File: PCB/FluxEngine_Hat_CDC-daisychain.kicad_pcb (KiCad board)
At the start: 2 copper layers, 83.3 x 24.1 mm, 3 parts, among them J1 CY8CKIT-059, P1 FDC_BUS_IBMPC, P2 FDC_BUS_CDC_DaisyChain

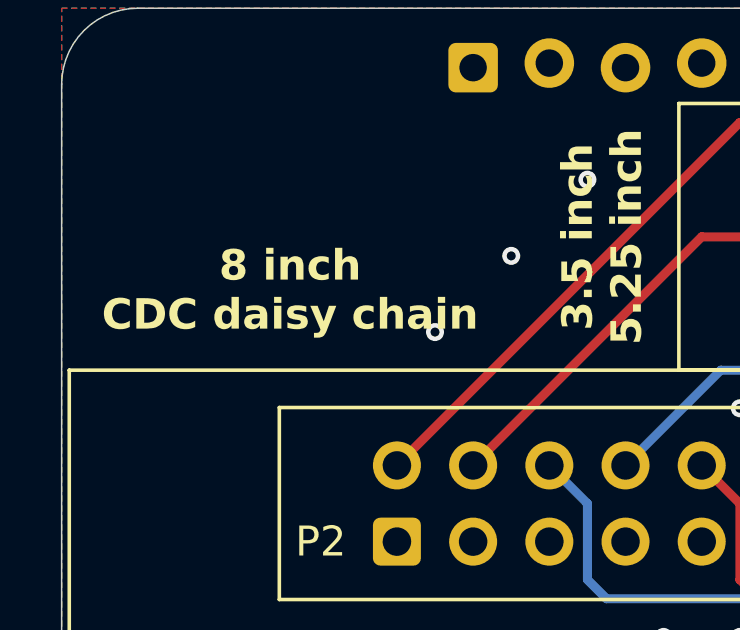
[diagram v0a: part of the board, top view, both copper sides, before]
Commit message: Combined CDC new & old standard interface
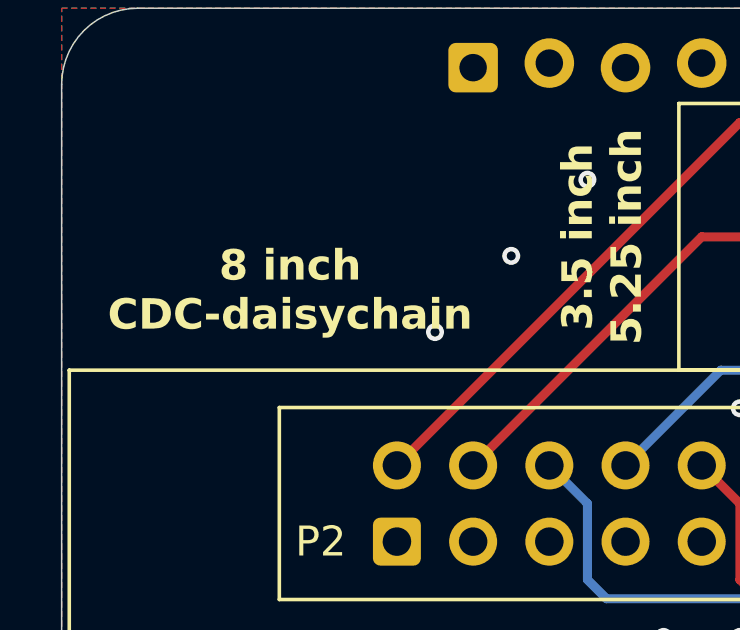
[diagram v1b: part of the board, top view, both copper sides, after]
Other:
- board text added: "8 inch CDC-daisychain"
- board text removed: "8 inch CDC daisy chain"
